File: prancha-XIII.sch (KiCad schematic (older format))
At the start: 21 parts

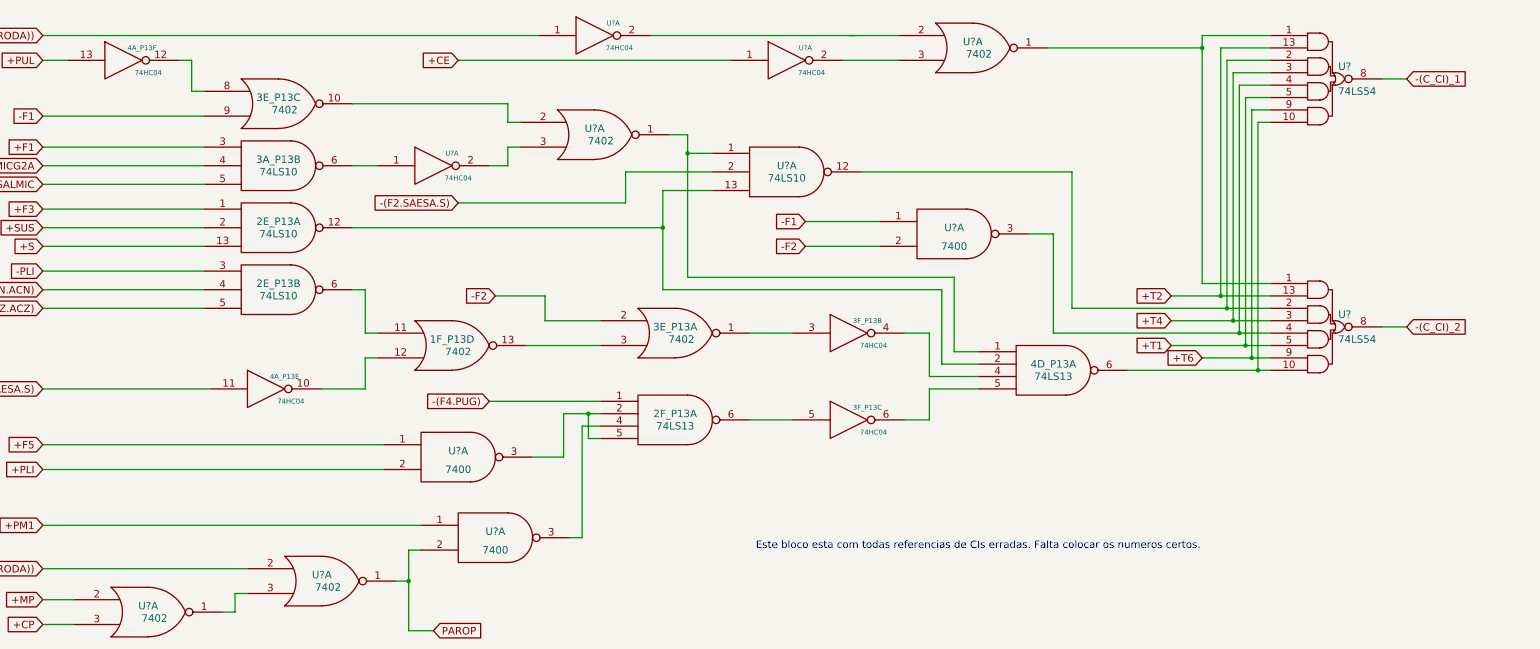
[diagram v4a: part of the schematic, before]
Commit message: revisei referencias e pinos dos chips de um pedaco incompleto de transcricao da prancha XIII
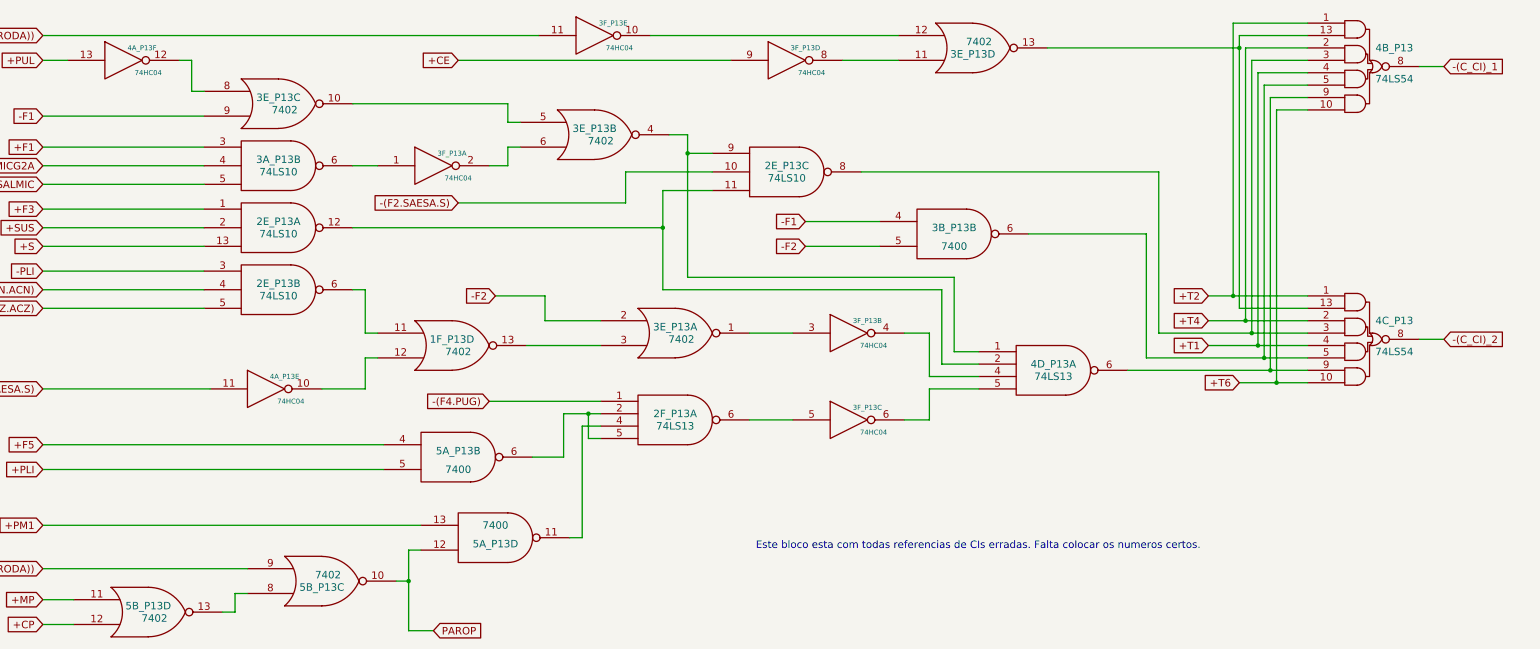
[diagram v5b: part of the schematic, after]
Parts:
- gave numbers to parts that had none: 8
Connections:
- net +(PARTIDA.(-RODA)): now also 3F_P13.11; no longer 3F_P13.1
- net +CE: now also 3F_P13.9; no longer 3F_P13.1
- net +CP: now also 5B_P13.12; no longer 5B_P13.3
- net +F5: now also 5A_P13.4; no longer 5A_P13.1
- net +MP: now also 5B_P13.11; no longer 5B_P13.2
- net +PLI: now also 5A_P13.5; no longer 5A_P13.2
- net +PM1: now also 5A_P13.13; no longer 5A_P13.1
- net +T1: now also 4B_P13.4, 4C_P13.4; no longer 4B_P13.5, 4C_P13.5
- net +T2: now also 4B_P13.1, 4C_P13.1; no longer 4B_P13.13, 4C_P13.13
- net +T4: now also 4B_P13.2, 4C_P13.2; no longer 4B_P13.3, 4C_P13.3
- net +T6: now also 4B_P13.10, 4C_P13.10; no longer 4B_P13.9, 4C_P13.9
- net -(F2.SAESA.S): now also 2E_P13.10; no longer 2E_P13.2
- net -(PARTIDA.(-RODA)): now also 5B_P13.9; no longer 5B_P13.2
- net -F1: now also 3B_P13.4; no longer 3B_P13.1
- net -F2: now also 3B_P13.5; no longer 3B_P13.2
- net PAROP: now also 5A_P13.12, 5B_P13.10; no longer 5A_P13.2, 5B_P13.1
- net at 3E_P13.10: now also 3E_P13.5; no longer 3E_P13.2
- net at 3F_P13.2: now also 3E_P13.6; no longer 3E_P13.3
- net at 2E_P13.12, 4D_P13.2: now also 2E_P13.11; no longer 2E_P13.13
- net at 2F_P13.2, 2F_P13.5: now also 5A_P13.6; no longer 5A_P13.3
- net at 2F_P13.4: now also 5A_P13.11; no longer 5A_P13.3
- new net: 2E_P13.9, 3E_P13.4, 4D_P13.1
- new net: 3E_P13.12, 3F_P13.10
- new net: 3E_P13.11, 3F_P13.8
- new net: 2E_P13.8, 4B_P13.3, 4C_P13.3
- new net: 3E_P13.13, 4B_P13.13, 4C_P13.13
- new net: 5B_P13.13, 5B_P13.8
- new net: 3B_P13.6, 4B_P13.5, 4C_P13.5
- new net: 4B_P13.9, 4C_P13.9, 4D_P13.6
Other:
- moved on the sheet: 4B_P13, 4C_P13
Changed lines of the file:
@@
 $EndComp
 $Comp
-L 7402 U?
-U 1 1 5772BFBB
+L 7402 3E_P13
+U 2 1 5772BFBB
 P 15200 2200
-F 0 "U?" H 15200 2250 60  0000 C CNN
+F 0 "3E_P13" H 15200 2250 60  0000 C CNN
 F 1 "7402" H 15250 2150 60  0000 C CNN
 F 2 "~" H 15200 2200 60  0000 C CNN
 F 3 "~" H 15200 2200 60  0000 C CNN
-	1    15200 2200
+	2    15200 2200
 	1    0    0    -1
 $EndComp
@@
 $EndComp
 $Comp
-L 74HC04 U?
+L 74HC04 3F_P13
 U 1 1 5772BFD0
 P 13900 2450
-F 0 "U?" H 14050 2550 40  0000 C CNN
+F 0 "3F_P13" H 14050 2550 40  0000 C CNN
 F 1 "74HC04" H 14100 2350 40  0000 C CNN
 F 2 "~" H 13900 2450 60  0000 C CNN
@@
 $EndComp
 $Comp
-L 74HC04 U?
-U 1 1 5772BFD6
+L 74HC04 3F_P13
+U 5 1 5772BFD6
 P 15200 1400
-F 0 "U?" H 15350 1500 40  0000 C CNN
+F 0 "3F_P13" H 15350 1500 40  0000 C CNN
 F 1 "74HC04" H 15400 1300 40  0000 C CNN
 F 2 "~" H 15200 1400 60  0000 C CNN
 F 3 "~" H 15200 1400 60  0000 C CNN
-	1    15200 1400
-	1    0    0    -1
-$EndComp
-$Comp
-L 74HC04 U?
-U 1 1 5772BFDC
+	5    15200 1400
+	1    0    0    -1
+$EndComp
+$Comp
+L 74HC04 3F_P13
+U 4 1 5772BFDC
 P 16750 1600
-F 0 "U?" H 16900 1700 40  0000 C CNN
+F 0 "3F_P13" H 16900 1700 40  0000 C CNN
 F 1 "74HC04" H 16950 1500 40  0000 C CNN
 F 2 "~" H 16750 1600 60  0000 C CNN
 F 3 "~" H 16750 1600 60  0000 C CNN
-	1    16750 1600
+	4    16750 1600
 	1    0    0    -1
 $EndComp
@@
 	14500 2100 14600 2100
 $Comp
-L 74LS10 U?
-U 1 1 5772C080
+L 74LS10 2E_P13
+U 3 1 5772C080
 P 16750 2500
-F 0 "U?" H 16750 2550 60  0000 C CNN
+F 0 "2E_P13" H 16750 2550 60  0000 C CNN
 F 1 "74LS10" H 16750 2450 60  0000 C CNN
 F 2 "~" H 16750 2500 60  0000 C CNN
 F 3 "~" H 16750 2500 60  0000 C CNN
-	1    16750 2500
+	3    16750 2500
 	1    0    0    -1
 $EndComp
@@
 	15950 2350 16150 2350
 Wire Wire Line
-	15950 2200 15950 3350
+	15950 2200 15950 2350
+Wire Wire Line
+	15950 2350 15950 3350
 Wire Wire Line
 	15950 2200 15800 2200
@@
 	14100 1600 16300 1600
 $Comp
-L 7402 U?
-U 1 1 579EC228
+L 7402 3E_P13
+U 4 1 579EC228
 P 18250 1500
-F 0 "U?" H 18250 1550 60  0000 C CNN
+F 0 "3E_P13" H 18250 1550 60  0000 C CNN
 F 1 "7402" H 18300 1450 60  0000 C CNN
 F 2 "~" H 18250 1500 60  0000 C CNN
 F 3 "~" H 18250 1500 60  0000 C CNN
-	1    18250 1500
-	1    0    0    -1
+	4    18250 1500
+	1    0    0    1
 $EndComp
 Wire Wire Line
 	17650 1600 17200 1600
 Wire Wire Line
-	15650 1400 17300 1400
-Wire Wire Line
-	17250 1400 17650 1400
-Wire Wire Line
 	13250 2950 15750 2950
 Wire Wire Line
-	15750 2650 15750 3450
+	15750 2650 15750 2950
+Wire Wire Line
+	15750 2950 15750 3450
 Text GLabel 14100 2750 0    60   Input ~ 0
 -(F2.SAESA.S)
@@
 	15250 4350 14350 4350
 $Comp
-L 7400 U?
-U 1 1 579EC4C0
+L 7400 5A_P13
+U 2 1 579EC4C0
 P 14100 4800
-F 0 "U?" H 14100 4850 60  0000 C CNN
+F 0 "5A_P13" H 14100 4850 60  0000 C CNN
 F 1 "7400" H 14100 4700 60  0000 C CNN
 F 2 "~" H 14100 4800 60  0000 C CNN
 F 3 "~" H 14100 4800 60  0000 C CNN
-	1    14100 4800
+	2    14100 4800
 	1    0    0    -1
 $EndComp
@@
 	13500 4900 10750 4900
 $Comp
-L 7400 U?
-U 1 1 579EC581
+L 7400 5A_P13
+U 4 1 579EC581
 P 14400 5450
-F 0 "U?" H 14400 5500 60  0000 C CNN
+F 0 "5A_P13" H 14400 5500 60  0000 C CNN
 F 1 "7400" H 14400 5350 60  0000 C CNN
 F 2 "~" H 14400 5450 60  0000 C CNN
 F 3 "~" H 14400 5450 60  0000 C CNN
-	1    14400 5450
-	1    0    0    -1
+	4    14400 5450
+	1    0    0    1
 $EndComp
 Wire Wire Line
@@
 	15100 5450 15000 5450
 $Comp
-L 7402 U?
-U 1 1 579EC5C9
+L 7402 5B_P13
+U 3 1 579EC5C9
 P 13000 5800
-F 0 "U?" H 13000 5850 60  0000 C CNN
+F 0 "5B_P13" H 13000 5850 60  0000 C CNN
 F 1 "7402" H 13050 5750 60  0000 C CNN
 F 2 "~" H 13000 5800 60  0000 C CNN
 F 3 "~" H 13000 5800 60  0000 C CNN
-	1    13000 5800
-	1    0    0    -1
-$EndComp
-$Comp
-L 7402 U?
-U 1 1 579EC5CF
+	3    13000 5800
+	1    0    0    1
+$EndComp
+$Comp
+L 7402 5B_P13
+U 4 1 579EC5CF
 P 11600 6050
-F 0 "U?" H 11600 6100 60  0000 C CNN
+F 0 "5B_P13" H 11600 6100 60  0000 C CNN
 F 1 "7402" H 11650 6000 60  0000 C CNN
 F 2 "~" H 11600 6050 60  0000 C CNN
 F 3 "~" H 11600 6050 60  0000 C CNN
-	1    11600 6050
+	4    11600 6050
 	1    0    0    -1
 $EndComp
@@
 	13800 5550 13700 5550
 Wire Wire Line
-	13700 5550 13700 6200
+	13700 5550 13700 5800
+Wire Wire Line
+	13700 5800 13700 6200
 Wire Wire Line
 	13700 5800 13600 5800
@@
 Connection ~ 13700 5800
 $Comp
-L 7400 U?
-U 1 1 579EC7D9
+L 7400 3B_P13
+U 2 1 579EC7D9
 P 18100 3000
-F 0 "U?" H 18100 3050 60  0000 C CNN
+F 0 "3B_P13" H 18100 3050 60  0000 C CNN
 F 1 "7400" H 18100 2900 60  0000 C CNN
 F 2 "~" H 18100 3000 60  0000 C CNN
 F 3 "~" H 18100 3000 60  0000 C CNN
-	1    18100 3000
+	2    18100 3000
 	1    0    0    -1
 $EndComp
@@
 	13350 3450 13250 3450
 $Comp
-L 74LS54 U?
+L 74LS54 4B_P13
 U 1 1 579ED1A1
-P 21100 1750
-F 0 "U?" H 21250 1850 60  0000 C CNN
-F 1 "74LS54" H 21350 1650 60  0000 C CNN
-F 2 "~" H 21100 1750 60  0000 C CNN
-F 3 "~" H 21100 1750 60  0000 C CNN
-	1    21100 1750
-	1    0    0    -1
-$EndComp
-$Comp
-L 74LS54 U?
+P 21400 1650
+F 0 "4B_P13" H 21650 1800 60  0000 C CNN
+F 1 "74LS54" H 21650 1550 60  0000 C CNN
+F 2 "~" H 21400 1650 60  0000 C CNN
+F 3 "~" H 21400 1650 60  0000 C CNN
+	1    21400 1650
+	1    0    0    -1
+$EndComp
+$Comp
+L 74LS54 4C_P13
 U 1 1 579ED1AE
-P 21100 3750
-F 0 "U?" H 21250 3850 60  0000 C CNN
-F 1 "74LS54" H 21350 3650 60  0000 C CNN
-F 2 "~" H 21100 3750 60  0000 C CNN
-F 3 "~" H 21100 3750 60  0000 C CNN
-	1    21100 3750
-	1    0    0    -1
-$EndComp
-Wire Wire Line
-	20650 2100 20550 2100
-Wire Wire Line
-	20550 2100 20550 4100
-Wire Wire Line
-	19500 4100 20650 4100
-Wire Wire Line
-	20100 4000 20650 4000
-Wire Wire Line
-	20500 4000 20500 2000
-Wire Wire Line
-	20500 2000 20650 2000
-Wire Wire Line
-	19850 3900 20650 3900
-Wire Wire Line
-	20450 3900 20450 1900
-Wire Wire Line
-	20450 1900 20650 1900
-Wire Wire Line
-	20650 1800 20400 1800
-Wire Wire Line
-	20400 1800 20400 3800
-Wire Wire Line
-	19850 3700 20650 3700
-Wire Wire Line
-	20350 3700 20350 1700
-Wire Wire Line
-	20350 1700 20650 1700
-Wire Wire Line
-	20650 1600 20300 1600
-Wire Wire Line
-	20300 1600 20300 3600
-Wire Wire Line
-	19050 3600 20650 3600
-Wire Wire Line
-	19850 3500 20650 3500
-Wire Wire Line
-	20250 3500 20250 1500
-Wire Wire Line
-	20250 1500 20650 1500
-Wire Wire Line
-	20650 1400 20100 1400
-Wire Wire Line
-	20100 1400 20100 3400
-Wire Wire Line
-	20100 3400 20650 3400
-Connection ~ 20550 4100
-Text GLabel 20100 4000 0    60   Input ~ 0
+P 21400 3850
+F 0 "4C_P13" H 21650 4000 60  0000 C CNN
+F 1 "74LS54" H 21650 3750 60  0000 C CNN
+F 2 "~" H 21400 3850 60  0000 C CNN
+F 3 "~" H 21400 3850 60  0000 C CNN
+	1    21400 3850
+	1    0    0    -1
+$EndComp
+Wire Wire Line
+	20950 1400 20400 1400
+Wire Wire Line
+	20400 1400 20400 1500
+Wire Wire Line
+	20400 1500 20400 3600
+Text GLabel 20400 4200 0    60   Input ~ 0
 +T6
-Connection ~ 20500 4000
-Text GLabel 19850 3900 0    60   Input ~ 0
+Text GLabel 20150 3900 0    60   Input ~ 0
 +T1
-Connection ~ 20450 3900
-Connection ~ 20400 3800
-Text GLabel 19850 3700 0    60   Input ~ 0
+Text GLabel 20150 3700 0    60   Input ~ 0
 +T4
-Connection ~ 20350 3700
-Wire Wire Line
-	18900 3800 20650 3800
-Text GLabel 19850 3500 0    60   Input ~ 0
+Text GLabel 20150 3500 0    60   Input ~ 0
 +T2
-Connection ~ 20250 3500
-Wire Wire Line
-	18900 3800 18900 3000
-Wire Wire Line
-	18900 3000 18700 3000
-Wire Wire Line
-	19050 3600 19050 2500
-Wire Wire Line
-	19050 2500 17350 2500
-Connection ~ 20300 3600
-Wire Wire Line
-	18850 1500 20100 1500
-Connection ~ 20100 1500
-Text GLabel 21750 3750 2    60   Input ~ 0
+Wire Wire Line
+	18700 3000 19650 3000
+Wire Wire Line
+	19750 2500 19750 3800
+Wire Wire Line
+	19750 2500 17350 2500
+Wire Wire Line
+	18850 1500 20400 1500
+Connection ~ 20400 1500
+Text GLabel 22050 3850 2    60   Input ~ 0
 -(C_CI)_2
 Wire Wire Line
-	21750 3750 21550 3750
-Text GLabel 21750 1750 2    60   Input ~ 0
+	22050 3850 21850 3850
+Text GLabel 22050 1650 2    60   Input ~ 0
 -(C_CI)_1
 Wire Wire Line
-	21550 1750 21750 1750
+	21850 1650 22050 1650
 Text Notes 16500 5550 0    60   ~ 0
 Este bloco esta com todas referencias de CIs erradas. Falta colocar os numeros certos.
@@
 $EndComp
 Wire Wire Line
-	15250 4450 14950 4450
+	14950 4450 15150 4450
+Wire Wire Line
+	15150 4450 15250 4450
 Wire Wire Line
 	14950 4450 14950 4800
@@
 	15150 4650 15150 4450
 Connection ~ 15150 4450
+Wire Wire Line
+	17650 1400 15650 1400
+Wire Wire Line
+	20400 3600 20950 3600
+Wire Wire Line
+	20150 3500 20350 3500
+Wire Wire Line
+	20350 3500 20950 3500
+Wire Wire Line
+	20150 3700 20450 3700
+Wire Wire Line
+	20450 3700 20950 3700
+Wire Wire Line
+	20150 3900 20550 3900
+Wire Wire Line
+	20550 3900 20950 3900
+Wire Wire Line
+	20400 4200 20700 4200
+Wire Wire Line
+	20700 4200 20950 4200
+Wire Wire Line
+	19500 4100 20650 4100
+Wire Wire Line
+	20650 4100 20950 4100
+Wire Wire Line
+	19750 3800 20500 3800
+Wire Wire Line
+	20500 3800 20950 3800
+Wire Wire Line
+	19650 4000 20600 4000
+Wire Wire Line
+	20600 4000 20950 4000
+Wire Wire Line
+	20350 3500 20350 1300
+Wire Wire Line
+	20350 1300 20950 1300
+Connection ~ 20350 3500
+Wire Wire Line
+	20950 1500 20450 1500
+Wire Wire Line
+	20450 1500 20450 3700
+Connection ~ 20450 3700
+Wire Wire Line
+	20950 1600 20500 1600
+Wire Wire Line
+	20500 1600 20500 3800
+Connection ~ 20500 3800
+Wire Wire Line
+	20950 1700 20550 1700
+Wire Wire Line
+	20550 1700 20550 3900
+Connection ~ 20550 3900
+Wire Wire Line
+	20600 1800 20950 1800
+Wire Wire Line
+	20600 1800 20600 4000
+Connection ~ 20600 4000
+Wire Wire Line
+	20650 4100 20650 1900
+Wire Wire Line
+	20650 1900 20950 1900
+Connection ~ 20650 4100
+Wire Wire Line
+	20950 2000 20700 2000
+Wire Wire Line
+	20700 2000 20700 4200
+Connection ~ 20700 4200
+Wire Wire Line
+	19650 3000 19650 4000
 $EndSCHEMATC

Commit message: mais um pouco...
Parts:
- added 1A_P13, 2A_P13, 2B_P13: 74HC04, ~, symbol 74HC04
- added 1C_P13, 1E_P13, 2C_P13, 5C_P13, 5C_P14: 7400, ~, symbol 7400
- added 1D_P13: 74LS10, ~, symbol 74LS10
- added unit 1 of 1F_P13
- added unit 3 of 1F_P13
- added unit 2 of 1F_P13
- added unit 2 of 2F_P13
- added unit 3 of 3A_P13
- added unit 6 of 3F_P13
- added unit 4 of 4A_P13
- added 4B_P?, 4C_P?: 74LS54, ~, symbol 74LS54
- added unit 3 of 5A_P13
- added unit 1 of 5B_P13
- added unit 2 of 5B_P13
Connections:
- net +CE: now also 3A_P13.9
- net +F1: now also 5A_P13.9
- net +F3: now also 5C_P14.4
- net +F5: now also 1F_P13.8
- net +PLI: now also 2A_P13.3
- net +SUS: now also 1F_P13.3
- net +T1: now also 5A_P13.10
- net +T2: now also 4B_P?.3, 4C_P?.3
- net +T4: now also 4B_P?.5, 4C_P?.5
- net +T6: now also 4B_P?.9, 4C_P?.9
- net -(F4.PUG): now also 5C_P13.3
- net -F1: now also 1A_P13.5
- net GND: now also 1A_P13.7 (GND), 1A_P13.7 (GND), 1A_P13.7 (GND), 1A_P13.7 (GND), 1A_P13.7 (GND), 1A_P13.7 (GND), 1C_P13.7 (GND), 1C_P13.7 (GND), 1C_P13.7 (GND), 1C_P13.7 (GND), 1D_P13.7 (GND), 1E_P13.7 (GND), 1F_P13.7 (GND), 1F_P13.7 (GND), 1F_P13.7 (GND), 2A_P13.7 (GND), 2A_P13.7 (GND), 2B_P13.7 (GND), 2B_P13.7 (GND), 2C_P13.7 (GND), 2C_P13.7 (GND), 2C_P13.7 (GND), 2F_P13.7 (GND), 3A_P13.7 (GND), 3F_P13.7 (GND), 4A_P13.7 (GND), 4B_P?.1, 4B_P?.13, 4B_P?.7 (GND), 4C_P?.1, 4C_P?.13, 4C_P?.7 (GND), 5A_P13.7 (GND), 5B_P13.6, 5B_P13.7 (GND), 5B_P13.7 (GND), 5C_P13.7 (GND), 5C_P13.7 (GND), 5C_P13.7 (GND), 5C_P14.7 (GND)
- net VCC: now also 1A_P13.14 (VCC), 1A_P13.14 (VCC), 1A_P13.14 (VCC), 1A_P13.14 (VCC), 1A_P13.14 (VCC), 1A_P13.14 (VCC), 1C_P13.14 (VCC), 1C_P13.14 (VCC), 1C_P13.14 (VCC), 1C_P13.14 (VCC), 1D_P13.14 (VCC), 1E_P13.14 (VCC), 1F_P13.14 (VCC), 1F_P13.14 (VCC), 1F_P13.14 (VCC), 2A_P13.14 (VCC), 2A_P13.14 (VCC), 2B_P13.14 (VCC), 2B_P13.14 (VCC), 2C_P13.14 (VCC), 2C_P13.14 (VCC), 2C_P13.14 (VCC), 2F_P13.14 (VCC), 3A_P13.14 (VCC), 3F_P13.14 (VCC), 4A_P13.14 (VCC), 4B_P?.14 (VCC), 4C_P?.14 (VCC), 5A_P13.14 (VCC), 5B_P13.14 (VCC), 5B_P13.14 (VCC), 5C_P13.14 (VCC), 5C_P13.14 (VCC), 5C_P13.14 (VCC), 5C_P14.14 (VCC)
- net -(PAROP.PMI): now reaches 2F_P13.4, 5A_P13.11
- net -(PAROP.PMI): now also 2F_P13.9
- net 4D_P13_6: now reaches 4B_P13.9, 4C_P13.9, 4D_P13.6
- net 4D_P13_6: now also 1E_P13.5
- new net: 2B_P13.13, 3A_P13.8
- new net: 1A_P13.2, 1C_P13.13
- new net: 1A_P13.4, 1C_P13.12
- new net: 1A_P13.6, 1C_P13.10
- new net: 1A_P13.12, 1C_P13.4
- new net: 1A_P13.10, 1C_P13.1
- new net: 1A_P13.8, 1C_P13.2
- new net: 1D_P13.1, 2C_P13.8
- new net: 1D_P13.12, 2B_P13.1
- new net: 1C_P13.8, 1D_P13.13
- new net: 1D_P13.2, 2C_P13.3
- new net: 1C_P13.11, 1C_P13.9
- new net: 1C_P13.3, 1C_P13.5
- new net: 1C_P13.6, 2C_P13.13
- new net: 2C_P13.11, 2C_P13.9
- new net: 1F_P13.1, 2C_P13.12
- new net: 2A_P13.2, 2C_P13.1
- new net: 2A_P13.4, 2C_P13.2
- new net: 2F_P13.10, 5C_P14.6
- new net: 1F_P13.10, 2F_P13.12
- new net: 2F_P13.13, 5B_P13.4
- new net: 2F_P13.8, 4B_P?.10, 4C_P?.10
- new net: 4B_P?.4, 4C_P?.4, 5B_P13.1
- new net: 4A_P13.9, 5C_P13.11
- new net: 4A_P13.8, 5C_P13.10
- new net: 3F_P13.12, 5C_P13.1
- new net: 1E_P13.6, 1F_P13.5
- new net +(CAC+SOM): 1A_P13.11
- new net +(F1+F2): 5B_P13.5
- new net +(PARTIDA(-RODA)): 3A_P13.11
- new net +5: 5C_P13.9
- new net +ARA: 1A_P13.9
- new net +F2: 2C_P13.10, 5C_P13.13
- new net +F4: 1F_P13.9
- new net +INDICE: 1A_P13.13
- new net +P(0-3)/M: 2B_P13.12
- new net +PUG: 1F_P13.2, 5C_P13.2
- new net +RI_(4-7)/M: 1F_P13.4
- new net +SAESA: 5C_P13.12
- new net +T12: 3A_P13.10
- new net +T56: 1E_P13.4
- new net +TRI: 1A_P13.3
- new net +TRO: 1A_P13.1
- new net -(C_RE)_1: 4B_P?.8
- new net -(C_RE)_2: 4C_P?.8
- new net -(C_RI): 5A_P13.8
- new net -(F2.SAESA.5): 5C_P13.8
- new net -(TRO+TRI): 5B_P13.2, 5C_P14.5
- new net -CF3: 2B_P13.2
- new net -F3: 5B_P13.3
- new net -F4: 1F_P13.6, 3F_P13.13
- new net -F5: 2A_P13.1
- new net 3E13: 4B_P?.2, 4C_P?.2
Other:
- note removed: "Este bloco esta com todas referencias de CIs erradas. Falta colocar os numeros certos."
- moved on the sheet: 1F_P13D, 2E_P13A, 2E_P13B, 2E_P13C, 2F_P13A, 3A_P13B, 3B_P13B, 3E_P13A, 3E_P13B, 3E_P13C, 3E_P13D, 3F_P13A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

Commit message: mais um pedaço do circuito (prancha 13)
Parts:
- added 1B_P13: 7400, ~, symbol 7400
- added unit 3 of 1D_P13
- added unit 2 of 1D_P13
- added unit 6 of 2A_P13
- added unit 3 of 2A_P13
- added unit 5 of 2B_P13
- added unit 2 of 2B_P13
- added unit 3 of 2B_P13
- added unit 4 of 2B_P13
- added unit 2 of 2C_P13
- added 2D_P13: 74LS51, symbol 74LS51
- added unit 1 of 3A_P13
- added unit 3 of 3B_P13 (x2)
- added unit 4 of 3B_P13
- added 3D_P13: 7402, ~, symbol 7402
- added unit 2 of 4A_P13
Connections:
- net +ARA: now also 1B_P13.1
- net +CP: now also 1B_P13.4
- net +F2: now also 3B_P13.13
- net +F3: now also 1B_P13.2, 2A_P13.6, 3A_P13.13, 3B_P13.9
- net +PUG: now also 2A_P13.13
- net +SUS: now also 3A_P13.1
- net -F3: now also 2A_P13.5, 3B_P13.8
- net -F4: now also 1D_P13.5
- net -PLI: now also 1D_P13.10
- net GND: now also 1B_P13.7 (GND), 1B_P13.7 (GND), 1B_P13.7 (GND), 1D_P13.7 (GND), 1D_P13.7 (GND), 2A_P13.7 (GND), 2A_P13.7 (GND), 2B_P13.7 (GND), 2B_P13.7 (GND), 2B_P13.7 (GND), 2B_P13.7 (GND), 2C_P13.7 (GND), 2D_P13.7 (GND), 3A_P13.7 (GND), 3B_P13.7 (GND), 3B_P13.7 (GND), 3B_P13.7 (GND), 3D_P13.7 (GND), 3D_P13.7 (GND), 4A_P13.7 (GND)
- net VCC: now also 1B_P13.14 (VCC), 1B_P13.14 (VCC), 1B_P13.14 (VCC), 1D_P13.14 (VCC), 1D_P13.14 (VCC), 2A_P13.14 (VCC), 2A_P13.14 (VCC), 2B_P13.14 (VCC), 2B_P13.14 (VCC), 2B_P13.14 (VCC), 2B_P13.14 (VCC), 2C_P13.14 (VCC), 2D_P13.14 (VCC), 3A_P13.14 (VCC), 3B_P13.14 (VCC), 3B_P13.14 (VCC), 3B_P13.14 (VCC), 3D_P13.14 (VCC), 3D_P13.14 (VCC), 4A_P13.14 (VCC)
- new net: 2A_P13.12, 2C_P13.4
- new net: 2B_P13.10, 2C_P13.5
- new net: 2C_P13.6, 3B_P13.10
- new net: 3B_P13.12, 3D_P13.1
- new net: 3D_P13.3, 4A_P13.4
- new net: 1D_P13.8, 4A_P13.3
- new net: 1B_P13.9, 3B_P13.10
- new net: 1B_P13.8, 2B_P13.3
- new net: 1D_P13.6, 2D_P13.3
- new net: 2B_P13.8, 2D_P13.4
- new net: 2B_P13.5, 2D_P13.6
- new net: 2B_P13.9, 3A_P13.12
- new net: 1B_P13.3, 1D_P13.3
- new net: 1B_P13.6, 1D_P13.4
- new net: 1B_P13.5, 3D_P13.13
- new net +(TRO+TRI): 2B_P13.11
- new net +RODA: 3D_P13.12
- new net +T23: 1B_P13.10, 2D_P13.2
- new net +T34: 2D_P13.5
- new net +U/R: 2B_P13.4
- new net +Z/R: 2B_P13.6
- new net -(CAC+SOM): 1D_P13.11
- new net -ARA: 1D_P13.9
- new net -CF4: 3B_P13.8
- new net -CF5: 3B_P13.11
- new net -INDICE: 3D_P13.2
- new net -PARTIDA: 3D_P13.11
- new net -PUG: 3B_P13.9
- new net -RDZ: 3A_P13.2
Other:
- note added: "-(CAC+SOM+PLI+ARA)\n"
- note added: "-CF5 = -F2.INDICE.(CAC+SOM+PLI+ARA)"
- note added: "INDICE.(CAC+SOM+PLI+ARA)"
